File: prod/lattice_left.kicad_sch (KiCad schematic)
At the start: 64 parts, among them J1 USB_C_Receptacle, J2 USB_C_Receptacle, U1 RP2040, U2 W25Q128JVS, U3 USBLC6-2SC6, U4 XC6206PxxxMR, Y1 Crystal_GND24_Small

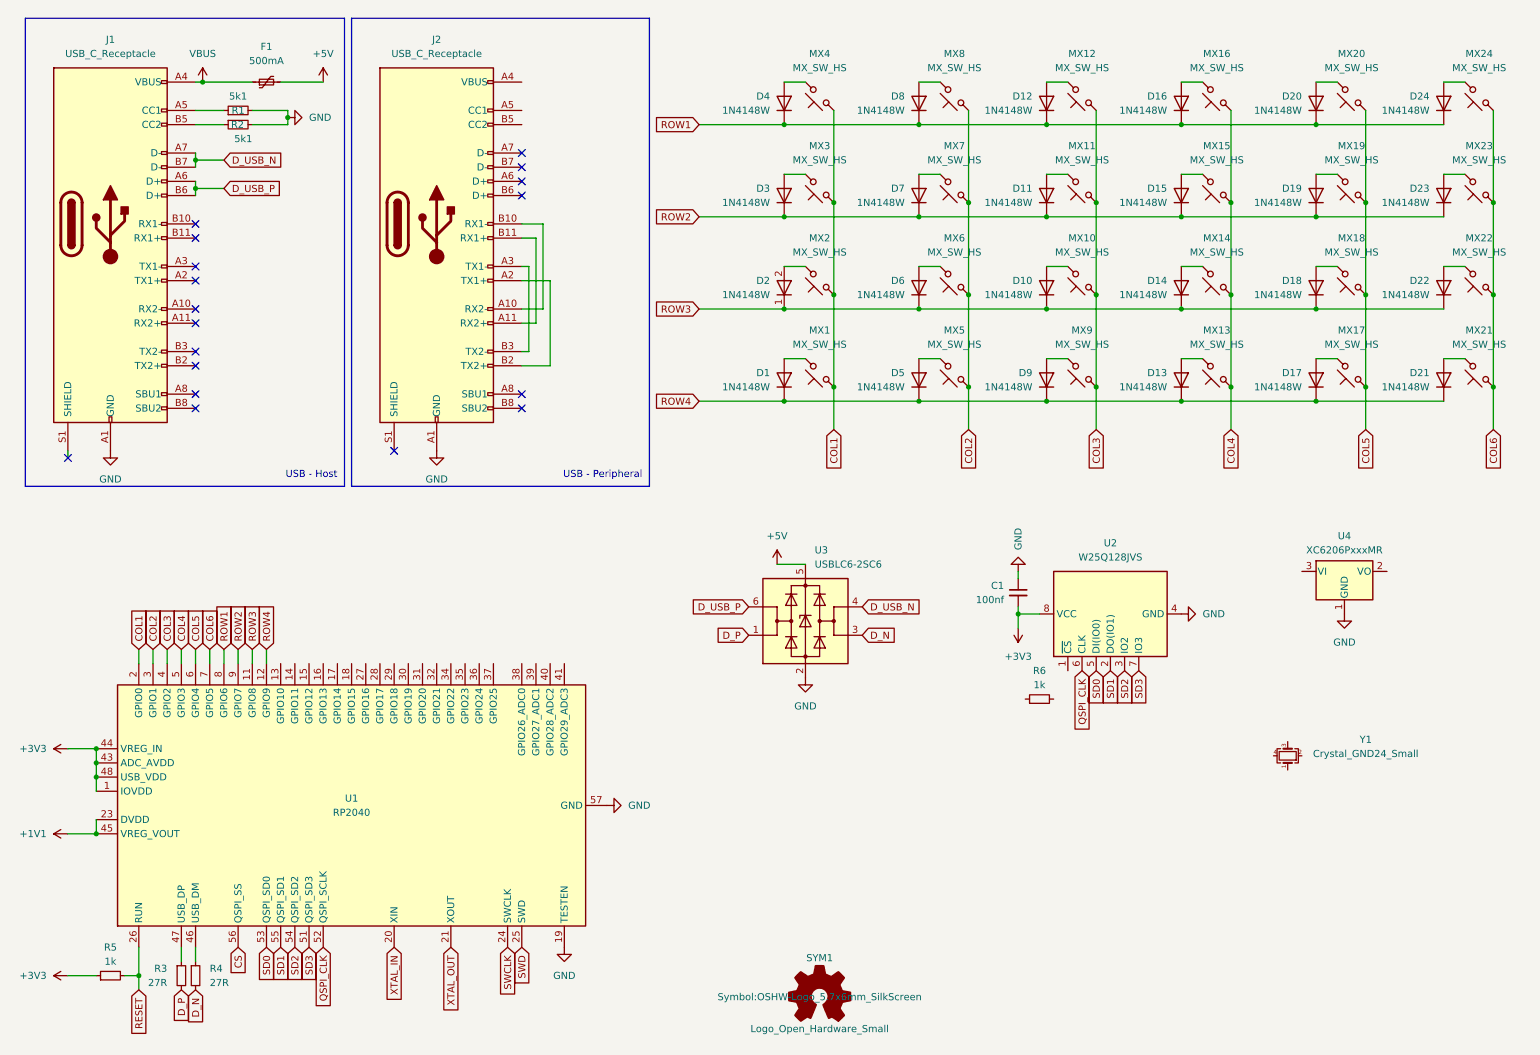
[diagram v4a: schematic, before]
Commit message: schematic done, most components placed
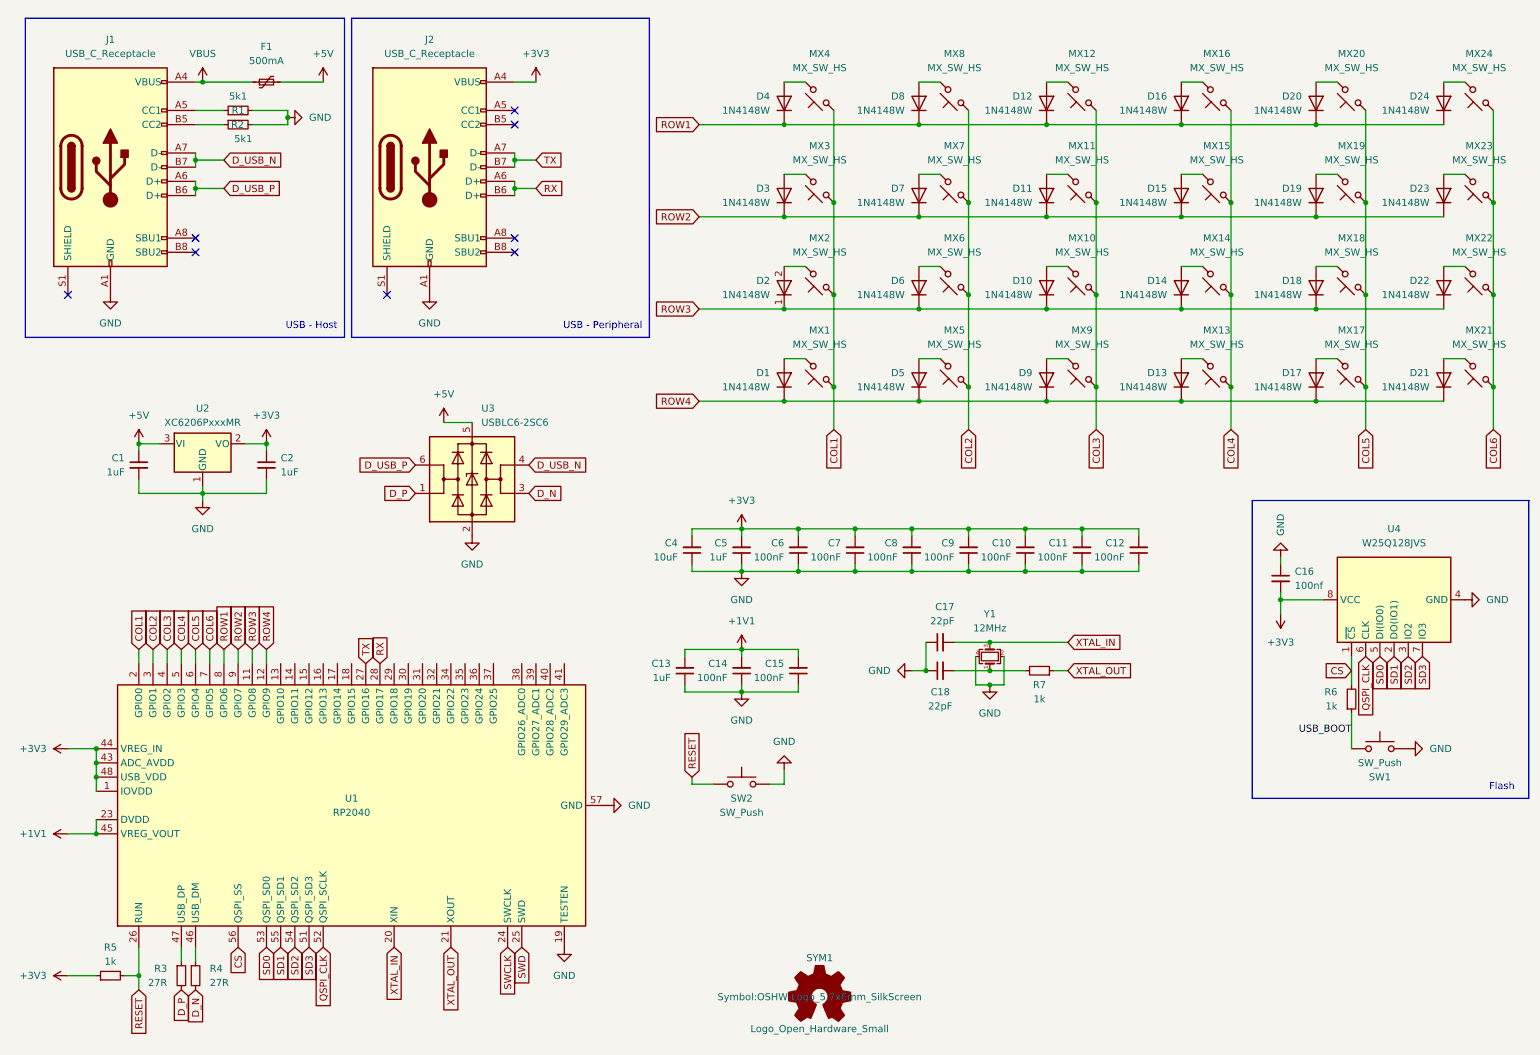
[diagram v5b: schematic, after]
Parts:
- added C1, C13, C2, C5: 1uF, Capacitor_SMD:C_0603_1608Metric, symbol Device:C_Small
- added C10, C11, C12, C14, C15, C6, C7, C8, C9: 100nF, Capacitor_SMD:C_0603_1608Metric, symbol Device:C_Small
- added C17, C18: 22pF, Capacitor_SMD:C_0603_1608Metric, symbol Device:C_Small
- added C4: 10uF, Capacitor_SMD:C_0603_1608Metric, symbol Device:C_Small
- added R7: 1k, Resistor_SMD:R_0603_1608Metric, symbol Device:R_Small
- added SW1, SW2: SW_Push, Button_Switch_SMD:SW_SPST_SKQG_WithStem, symbol Switch:SW_Push
- C16: renamed from C1; footprint (none) -> Capacitor_SMD:C_0603_1608Metric
- J1, J2: symbol Connector:USB_C_Receptacle -> Connector:USB_C_Receptacle_USB2.0_16P
- R3, R4, R5, R6: footprint (none) -> Resistor_SMD:R_0603_1608Metric
- Y1: value Crystal_GND24_Small -> 12MHz
- renumbered U4 to U2, U2 to U4
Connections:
- net +1V1: now also C13.2, C14.2, C15.2
- net +3V3: now also J2.A4 (VBUS), J2.A9 (VBUS), J2.B4 (VBUS), J2.B9 (VBUS), U2.2 (VO), C10.2, C11.2, C12.2, C2.1, C4.2, C5.2, C6.2, C7.2, C8.2, C9.2
- net +5V: now also U2.3 (VI), C1.1
- net CS: now also R6.2, U4.1 (~{CS})
- net GND: now also Y1.2, Y1.4, C1.2, C10.1, C11.1, C12.1, C13.1, C14.1, C15.1, C17.1, C18.1, C2.2, C4.1, C5.1, C6.1, C7.1, C8.1, C9.1, SW1.1, SW2.1
- net RESET: now also SW2.2
- net XTAL_IN: now also Y1.3, C17.2
- net XTAL_OUT: now also R7.1
- net USB_BOOT: now reaches R6.1
- net USB_BOOT: now also SW1.2
- net RX: now reaches J2.A6 (D+)
- net RX: now also J2.B6 (D+), U1.28 (GPIO17)
- net TX: now reaches J2.A7 (D-)
- net TX: now also J2.B7 (D-), U1.27 (GPIO16)
- net at Y1.1: now also C18.2, R7.2
- no-connect marks 18 -> 8
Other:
- note added: "Flash"
- moved on the sheet: C16, R6, U2, U3, U4, Y1

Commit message: components placed
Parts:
- removed SW2: SW_Push, Button_Switch_SMD:SW_SPST_SKQG_WithStem, symbol Switch:SW_Push
- added SW1: SW_Push, Button_Switch_SMD:SW_SPST_SKQG_WithStem, symbol Switch:SW_Push
- renumbered C8 to C10, C9 to C11, C10 to C12, C11 to C13, C12 to C14, C13 to C15, C14 to C16, C15 to C17, C16 to C3, C17 to C4, C18 to C5, C4 to C6, C5 to C7, C6 to C8, C7 to C9, SW1 to SW2
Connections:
- net GND: now also SW1.1
- net RESET: now also SW1.2
- net USB_BOOT renamed BOOT
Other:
- note added: "Buttons"
- note added: "Crystal Oscillator"
- note added: "Decoupling Capacitors"
- note added: "Power - Transient Voltage Suppressor"
- note added: "Power - Volatage Regulator"
- note added: "RP2040"
- note added: "Switch Matrix"
- moved on the sheet: C1, C10, C11, C12, C13, C14, C15, C16, C17, C2, C3, C4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

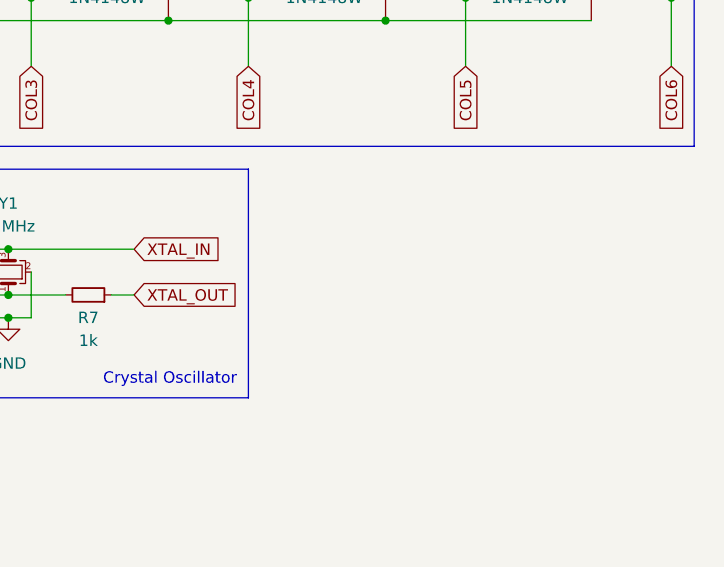
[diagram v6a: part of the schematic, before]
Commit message: adding breakout header
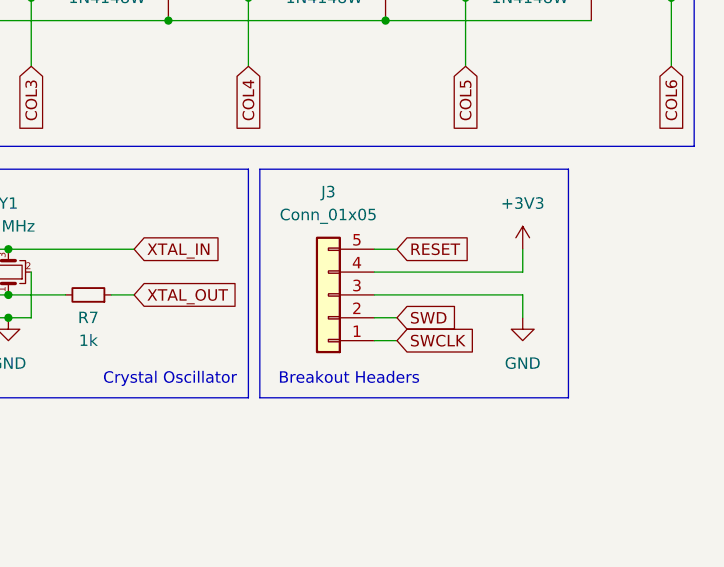
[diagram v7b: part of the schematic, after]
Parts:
- added J3: Conn_01x05, Connector_PinSocket_2.54mm:PinSocket_1x05_P2.54mm_Vertical, symbol Connector_Generic:Conn_01x05
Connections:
- net +3V3: now also J3.4 (Pin_4)
- net GND: now also J3.3 (Pin_3)
- net RESET: now also J3.5 (Pin_5)
- net SWCLK: now also J3.1 (Pin_1)
- net SWD: now also J3.2 (Pin_2)
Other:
- note added: "Breakout Headers"
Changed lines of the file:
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@@
+    (stroke (width 0) (type default))
+  )
+  (wire (pts (xy 264.16 105.41) (xy 264.16 102.87))
     (stroke (width 0) (type default))
   )
@@
     (stroke (width 0) (type default))
   )
+  (wire (pts (xy 247.65 113.03) (xy 250.19 113.03))
+    (stroke (width 0) (type default))
+  )
   (wire (pts (xy 209.55 105.41) (xy 209.55 110.49))
     (stroke (width 0) (type default))
@@
     (stroke (width 0) (type default))
   )
+  (wire (pts (xy 247.65 110.49) (xy 250.19 110.49))
+    (stroke (width 0) (type default))
+  )
   (wire (pts (xy 200.66 156.21) (xy 210.82 156.21))
     (stroke (width 0) (type default))
@@
     (stroke (width 0) (type default))
   )
+  (wire (pts (xy 247.65 107.95) (xy 264.16 107.95))
+    (stroke (width 0) (type default))
+  )
   (wire (pts (xy 36.83 92.71) (xy 48.26 92.71))
     (stroke (width 0) (type default))
@@
     (stroke (width 0) (type default))
   )
+  (wire (pts (xy 247.65 102.87) (xy 250.19 102.87))
+    (stroke (width 0) (type default))
+  )
   (wire (pts (xy 180.34 148.59) (xy 190.5 148.59))
     (stroke (width 0) (type default))
@@
     (stroke (width 0) (type default))
   )
+  (wire (pts (xy 247.65 105.41) (xy 264.16 105.41))
+    (stroke (width 0) (type default))
+  )
   (wire (pts (xy 46.99 25.4) (xy 55.88 25.4))
     (stroke (width 0) (type default))
@@
     (stroke (width 0) (type default))
   )
+  (wire (pts (xy 264.16 107.95) (xy 264.16 110.49))
+    (stroke (width 0) (type default))
+  )
   (wire (pts (xy 77.47 81.28) (xy 82.55 81.28))
     (stroke (width 0) (type default))
@@
     (fill (type none))
   )
+  (rectangle (start 234.95 93.98) (end 269.24 119.38)
+    (stroke (width 0) (type default))
+    (fill (type none))
+  )
   (rectangle (start 13.97 13.97) (end 13.97 13.97)
     (stroke (width 0) (type default))
@@
   )
   (text "Switch Matrix" (at 143.51 90.17 0)
+    (effects (font (size 1.27 1.27)) (justify right bottom))
+  )
+  (text "Breakout Headers" (at 252.73 118.11 0)
     (effects (font (size 1.27 1.27)) (justify right bottom))
   )
@@
     )
   )
+  (global_label "RESET" (shape input) (at 250.19 102.87 0) (fields_autoplaced)
+    (effects (font (size 1.27 1.27)) (justify left))
+    (property "Intersheetrefs" "${INTERSHEET_REFS}" (at 258.9203 102.87 0)
+      (effects (font (size 1.27 1.27)) (justify left) hide)
+    )
+  )
   (global_label "COL2" (shape input) (at 186.69 82.55 270) (fields_autoplaced)
     (effects (font (size 1.27 1.27)) (justify right))
@@
     )
   )
+  (global_label "SWD" (shape input) (at 250.19 110.49 0) (fields_autoplaced)
+    (effects (font (size 1.27 1.27)) (justify left))
+    (property "Intersheetrefs" "${INTERSHEET_REFS}" (at 257.1061 110.49 0)
+      (effects (font (size 1.27 1.27)) (justify left) hide)
+    )
+  )
   (global_label "COL1" (shape input) (at 162.56 82.55 270) (fields_autoplaced)
     (effects (font (size 1.27 1.27)) (justify right))
@@
     )
   )
+  (global_label "SWCLK" (shape input) (at 250.19 113.03 0) (fields_autoplaced)
+    (effects (font (size 1.27 1.27)) (justify left))
+    (property "Intersheetrefs" "${INTERSHEET_REFS}" (at 259.4042 113.03 0)
+      (effects (font (size 1.27 1.27)) (justify left) hide)
+    )
+  )
   (global_label "CS" (shape input) (at 53.34 180.34 270) (fields_autoplaced)
     (effects (font (size 1.27 1.27)) (justify right))
@@
         (path "/7175bad1-6d67-4925-85bf-3e5286dbd285"
           (reference "C11") (unit 1)
+        )
+      )
+    )
+  )
+  (symbol (lib_id "power:+3V3") (at 264.16 102.87 0) (unit 1)
+    (in_bom yes) (on_board yes) (dnp no) (fields_autoplaced)
+    (property "Reference" "#PWR027" (at 264.16 106.68 0)
+      (effects (font (size 1.27 1.27)) hide)
+    )
+    (property "Value" "+3V3" (at 264.16 97.79 0)
+      (effects (font (size 1.27 1.27)))
+    )
+    (property "Footprint" "" (at 264.16 102.87 0)
+      (effects (font (size 1.27 1.27)) hide)
+    )
+    (property "Datasheet" "" (at 264.16 102.87 0)
+      (effects (font (size 1.27 1.27)) hide)
+    )
+    (pin "1")
+    (instances
+      (project "lattice_left"
+        (path "/7175bad1-6d67-4925-85bf-3e5286dbd285"
+          (reference "#PWR027") (unit 1)
         )
       )
@@
     )
   )
+  (symbol (lib_id "power:GND") (at 264.16 110.49 0) (unit 1)
+    (in_bom yes) (on_board yes) (dnp no) (fields_autoplaced)
+    (property "Reference" "#PWR029" (at 264.16 116.84 0)
+      (effects (font (size 1.27 1.27)) hide)
+    )
+    (property "Value" "GND" (at 264.16 115.57 0)
+      (effects (font (size 1.27 1.27)))
+    )
+    (property "Footprint" "" (at 264.16 110.49 0)
+      (effects (font (size 1.27 1.27)) hide)
+    )
+    (property "Datasheet" "" (at 264.16 110.49 0)
+      (effects (font (size 1.27 1.27)) hide)
+    )
+    (pin "1")
+    (instances
+      (project "lattice_left"
+        (path "/7175bad1-6d67-4925-85bf-3e5286dbd285"
+          (reference "#PWR029") (unit 1)
+        )
+      )
+    )
+  )
   (symbol (lib_id "marbastlib-mx:MX_SW_HS") (at 184.15 55.88 180) (unit 1)
     (in_bom yes) (on_board yes) (dnp no) (fields_autoplaced)
@@
         )
       )
+    )
+  )
+  (symbol (lib_id "Connector_Generic:Conn_01x05") (at 242.57 107.95 180) (unit 1)
+    (in_bom yes) (on_board yes) (dnp no) (fields_autoplaced)
+    (property "Reference" "J3" (at 242.57 96.52 0)
+      (effects (font (size 1.27 1.27)))
+    )
+    (property "Value" "Conn_01x05" (at 242.57 99.06 0)
+      (effects (font (size 1.27 1.27)))
+    )
+    (property "Footprint" "Connector_PinSocket_2.54mm:PinSocket_1x05_P2.54mm_Vertical" (at 242.57 107.95 0)
+      (effects (font (size 1.27 1.27)) hide)
+    )
+    (property "Datasheet" "~" (at 242.57 107.95 0)
+      (effects (font (size 1.27 1.27)) hide)
+    )
+    (pin "3")
+    (pin "4")
+    (pin "2")
+    (pin "1")
+    (pin "5")
+    (instances
+      (project "lattice_left"
+        (path "/7175bad1-6d67-4925-85bf-3e5286dbd285"
+          (reference "J3") (unit 1)
+        )
+      )
